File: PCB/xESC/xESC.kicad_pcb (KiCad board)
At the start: 2 copper layers, 58 x 29 mm, 74 parts, among them J1 Conn_01x05_Male, J2 Conn_01x03_Male, J3 Conn_01x03_Male, J4 Conn_01x03_Male, Q1 BSC440N10NS3G, Q2 BSC440N10NS3G, Q3 BSC440N10NS3G, Q4 BSC440N10NS3G, Q5 BSC440N10NS3G, Q6 BSC440N10NS3G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

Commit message: fixed silkscreen
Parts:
- added D3: 50V, Diode_SMD:D_SOT-23_ANK, B.Cu at (169.1, 56.6)
- added D4: LED, LED_SMD:LED_0805_2012Metric_Pad1.15x1.40mm_HandSolder, F.Cu at (200.6, 40.7)
- added JP1: SolderJumper_2_Open, Jumper:SolderJumper-2_P1.3mm_Open_Pad1.0x1.5mm, F.Cu at (197.1, 45.2)
- added R19: 10kR, Resistor_SMD:R_0805_2012Metric, B.Cu at (179.9, 47.2)
- added R20: 1kR, Resistor_SMD:R_0805_2012Metric, B.Cu at (179.9, 42.8)
- added R21: 150R, Resistor_SMD:R_0805_2012Metric, F.Cu at (199.9, 37.2)
- C2, C3, C5: value c? -> 470nF@16V
- R7: value 30mR - 1W -> 3mR - 1W
- moved R8 0.40 mm to (196.8, 44.6)
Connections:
- U1 pad 22: (no net) -> Net-(R19-Pad2)
- U2 pad 9: (no net) -> Net-(JP1-Pad2)
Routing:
- net Net-(R19-Pad2): track 0.00 -> 43.5 mm, vias 0 -> 1
- net /DRV_ENABLE: track 27.9 -> 37.8 mm
- net /V_M: track 60.4 -> 66.5 mm
- net VCC: track 104.8 -> 110.5 mm
- net Net-(JP1-Pad2): track 0.00 -> 4.39 mm
- net Net-(D4-Pad1): track 0.00 -> 3.14 mm
- net /MISO: track 30.2 -> 28.7 mm
- net /DRV_SS: track 19.4 -> 17.8 mm
- net /INPUT_PWM: track 24.7 -> 23.2 mm
- net /MOSI: track 29.1 -> 27.9 mm
- net /Power/LS_V: track 30.8 -> 31.9 mm
- net /HALL_V: track 16.8 -> 17.5 mm
- net /I_SENSE: track 23.7 -> 23.2 mm
- net /INPUT_ANALOG: track 19.5 -> 20.0 mm
- net GND: vias 72 -> 71

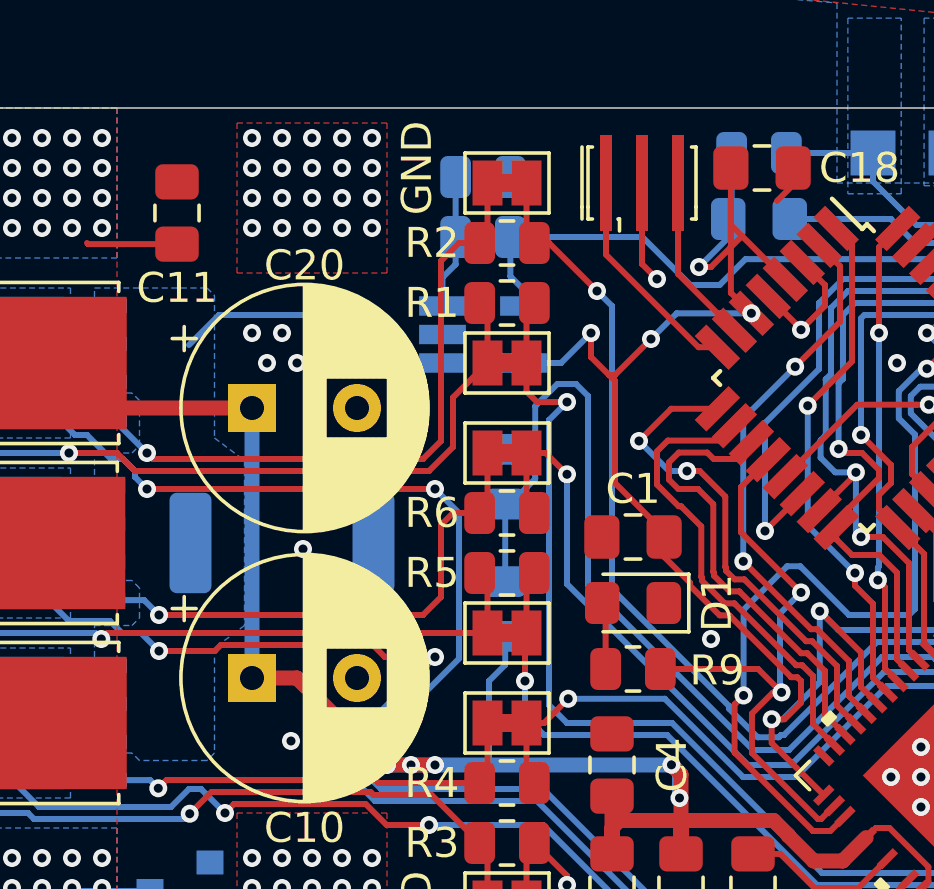
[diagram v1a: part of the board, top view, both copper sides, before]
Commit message: changed current sense amplifier to MCP601R, added values for current sense resistors
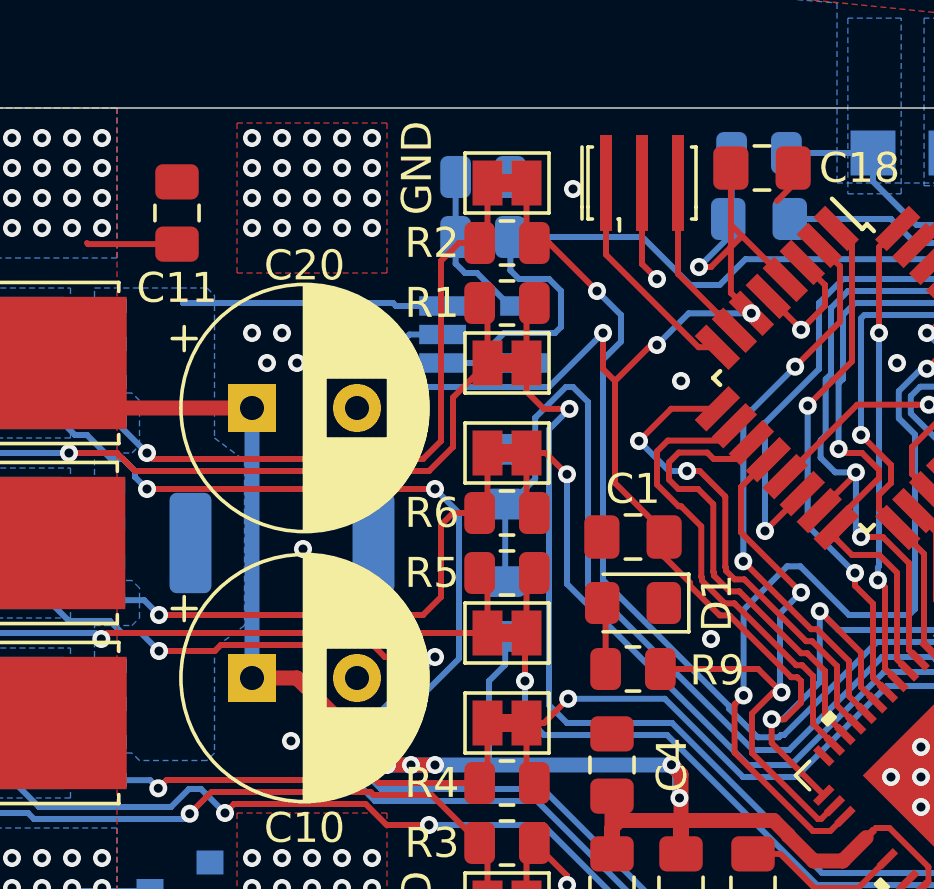
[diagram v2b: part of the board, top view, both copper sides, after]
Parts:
- R18: value 1kR -> 10kR
- U3: value LMV321 -> MCP601R
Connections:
- U3 pad 1: /Power/BridgeMosfets/GND -> /I_SENSE
- U3 pad 2: GND -> VCC
- U3 pad 3: Net-(R10-Pad1) -> /Power/BridgeMosfets/GND
- U3 pad 4: /I_SENSE -> Net-(R10-Pad1)
- U3 pad 5: VCC -> GND
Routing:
- net VCC: track 110.5 -> 117.8 mm
- net /I_SENSE: track 23.2 -> 30.2 mm
- net Net-(R10-Pad1): track 4.48 -> 5.74 mm
- net /Power/BridgeMosfets/GND: track 9.53 -> 8.89 mm
- net GND: vias 71 -> 73

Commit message: Update xESC.kicad_pcb
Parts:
- R10: value R -> 1.5kR
- R11: value R -> 150kR

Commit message: added gerbers
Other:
- board text added: "JLCJLCJLCJLC"
